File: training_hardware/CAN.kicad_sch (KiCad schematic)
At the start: 7 parts, among them U2 OKI

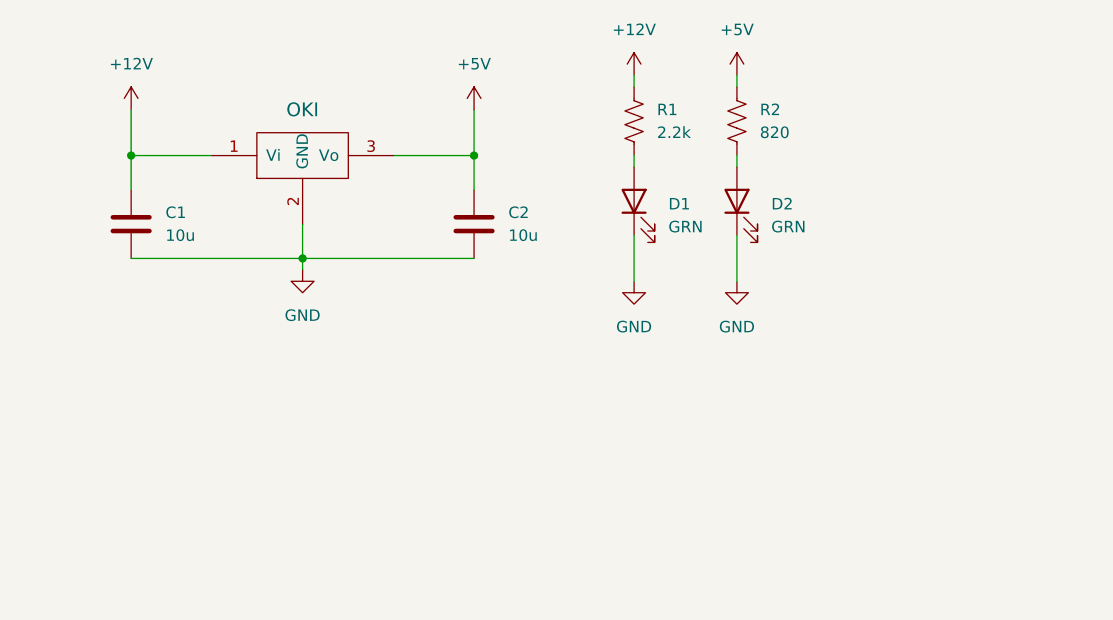
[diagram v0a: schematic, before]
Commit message: Add CAN Transceiver
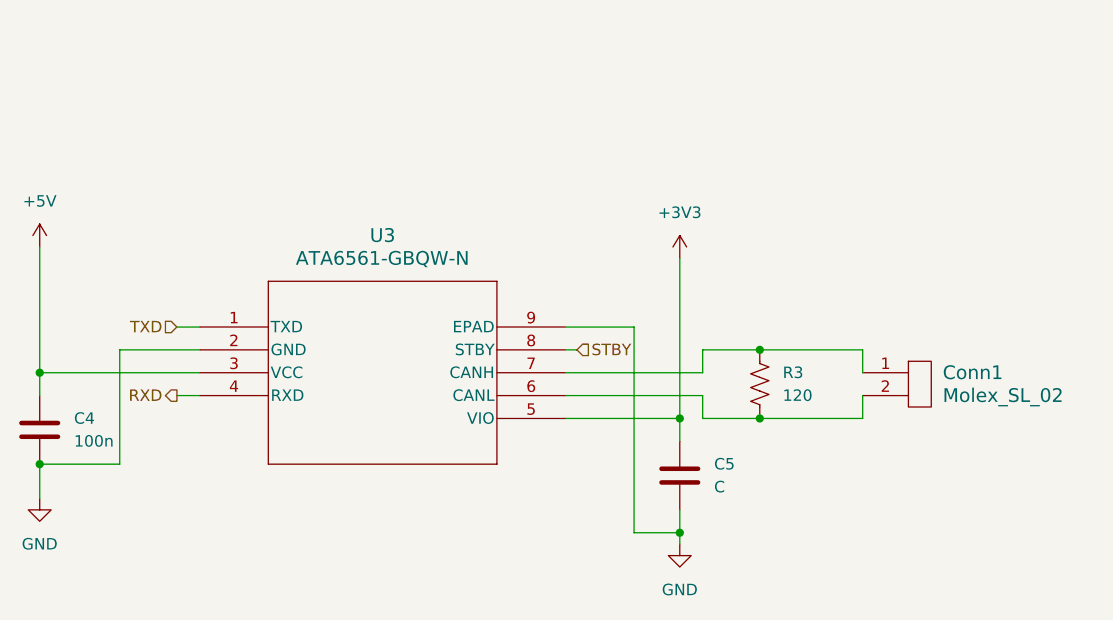
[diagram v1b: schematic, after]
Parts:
- removed C1, C2: 10u, symbol Device:C
- removed D1, D2: GRN, symbol Device:LED
- removed R1: 2.2k, symbol Device:R_US
- removed R2: 820, symbol Device:R_US
- removed U2: OKI, symbol MRDT_Devices:OKI
- added C4: 100n, symbol Device:C
- added C5: C, symbol Device:C
- added Conn1: Molex_SL_02, symbol MRDT_Connectors:Molex_SL_02
- added R3: 120, symbol Device:R_US
- added U3: ATA6561-GBQW-N, VDFN8_3X3_MCH, symbol 2026_training_hardware:ATA6561-GBQW-N
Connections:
- net +5V: now also C4.1, U3.3 (VCC)
- net GND: now also C4.2, C5.2, U3.2 (GND), U3.9 (EPAD)
- new net: Conn1.1, R3.1, U3.7 (CANH)
- new net: Conn1.2, R3.2, U3.6 (CANL)
- new net +3V3: C5.1, U3.5 (VIO)
- new net RXD: U3.4 (RXD)
- new net STBY: U3.8 (STBY)
- new net TXD: U3.1 (TXD)

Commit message: Layout Training
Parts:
- removed U3: ATA6561-GBQW-N, VDFN8_3X3_MCH, symbol 2026_training_hardware:ATA6561-GBQW-N
- added U3: ATA6561-GAQW-N, 2026_Training_Hardware:SOIC8_4P9X3P9MC_MCH-L, symbol 2026_training_hardware:ATA6561-GAQW-N
- C4: footprint (none) -> Capacitor_SMD:C_0603_1608Metric_Pad1.08x0.95mm_HandSolder
- C5: footprint (none) -> Capacitor_SMD:C_0603_1608Metric
- Conn1: footprint (none) -> MRDT_Connectors:MOLEX_SL_02_Vertical
- R3: footprint (none) -> Resistor_SMD:R_0603_1608Metric_Pad0.98x0.95mm_HandSolder
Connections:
- net +3V3: now also U3.5 (VIO)
- net +5V: now also U3.3 (VCC)
- net GND: now also U3.2 (GND), U3.9 (EPAD)
- net RXD: now also U3.4 (RXD)
- net STBY: now also U3.8 (STBY)
- net TXD: now also U3.1 (TXD)
- net at Conn1.1, R3.1: now also U3.7 (CANH)
- net at Conn1.2, R3.2: now also U3.6 (CANL)
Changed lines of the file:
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@@
 			)
 		)
-		(property "Footprint" ""
+		(property "Footprint" "MRDT_Connectors:MOLEX_SL_02_Vertical"
 			(at 204.47 99.06 0)
 			(effects
@@
 			)
 		)
-		(property "Footprint" ""
+		(property "Footprint" "Capacitor_SMD:C_0603_1608Metric_Pad1.08x0.95mm_HandSolder"
 			(at 108.9152 102.87 0)
 			(effects
@@
 	)
 	(symbol
-		(lib_id "2026_training_hardware:ATA6561-GBQW-N")
+		(lib_id "2026_training_hardware:ATA6561-GAQW-N")
 		(at 125.73 87.63 0)
 		(unit 1)
@@
 			)
 		)
-		(property "Value" "ATA6561-GBQW-N"
+		(property "Value" "ATA6561-GAQW-N"
 			(at 146.05 80.01 0)
 			(effects
@@
 			)
 		)
-		(property "Footprint" "VDFN8_3X3_MCH"
+		(property "Footprint" "2026_Training_Hardware:SOIC8_4P9X3P9MC_MCH-L"
 			(at 125.73 87.63 0)
 			(effects
@@
 			)
 		)
+		(pin "1"
+		)
+		(pin "3"
+		)
+		(pin "5"
+		)
+		(pin "7"
+		)
+		(pin "2"
+		)
 		(pin "8"
 		)
-		(pin "2"
-		)
 		(pin "9"
 		)
-		(pin "3"
+		(pin "6"
 		)
 		(pin "4"
-		)
-		(pin "6"
-		)
-		(pin "7"
-		)
-		(pin "5"
-		)
-		(pin "1"
 		)
 		(instances
@@
 			)
 		)
-		(property "Footprint" ""
+		(property "Footprint" "Resistor_SMD:R_0603_1608Metric_Pad0.98x0.95mm_HandSolder"
 			(at 188.976 94.234 90)
 			(effects
@@
 			)
 		)
-		(property "Footprint" ""
+		(property "Footprint" "Capacitor_SMD:C_0603_1608Metric"
 			(at 180.0352 107.95 0)
 			(effects
